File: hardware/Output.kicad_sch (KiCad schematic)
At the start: 26 parts, among them J11 Conn_Coaxial, J12 Conn_Coaxial, J13 Conn_Coaxial, J14 Conn_Coaxial, J15 Conn_Coaxial, J16 Conn_Coaxial, J17 Conn_Coaxial, J18 Conn_Coaxial, U31 74LVCH2T45DC, U32 74LVCH2T45DC

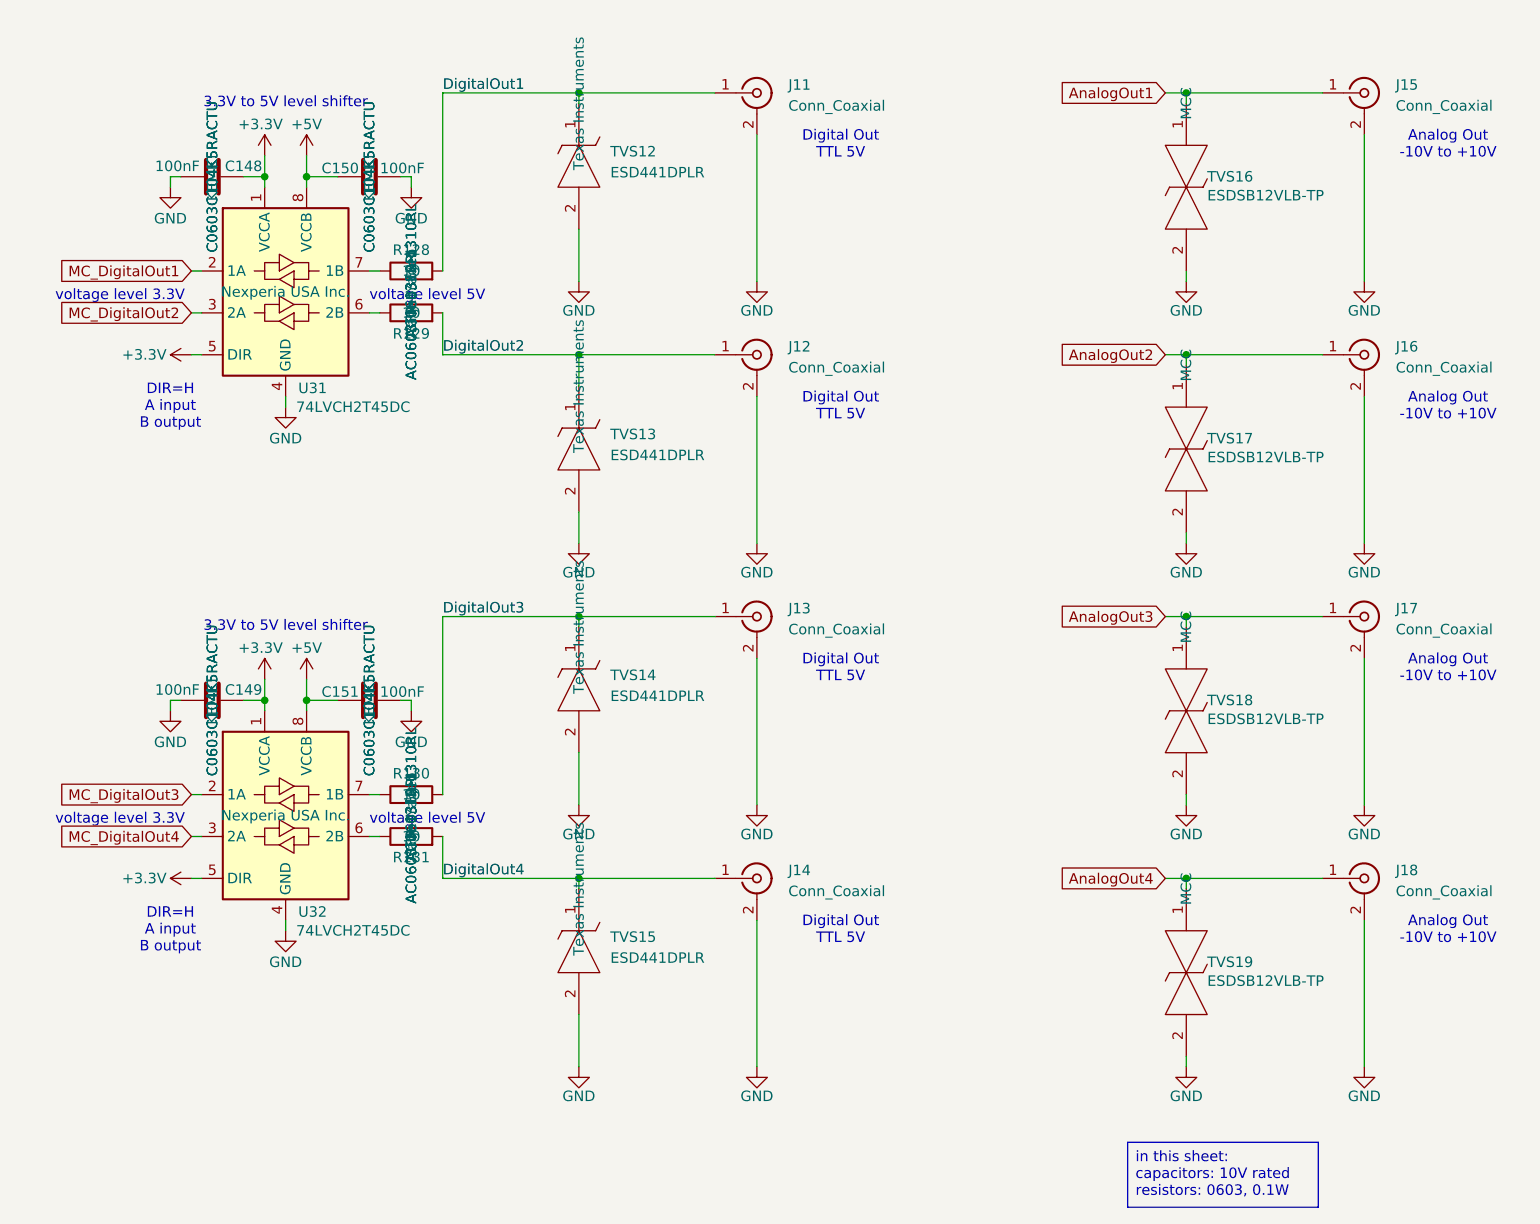
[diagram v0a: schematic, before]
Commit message: Not necessary text is hidden + BOM on schematic
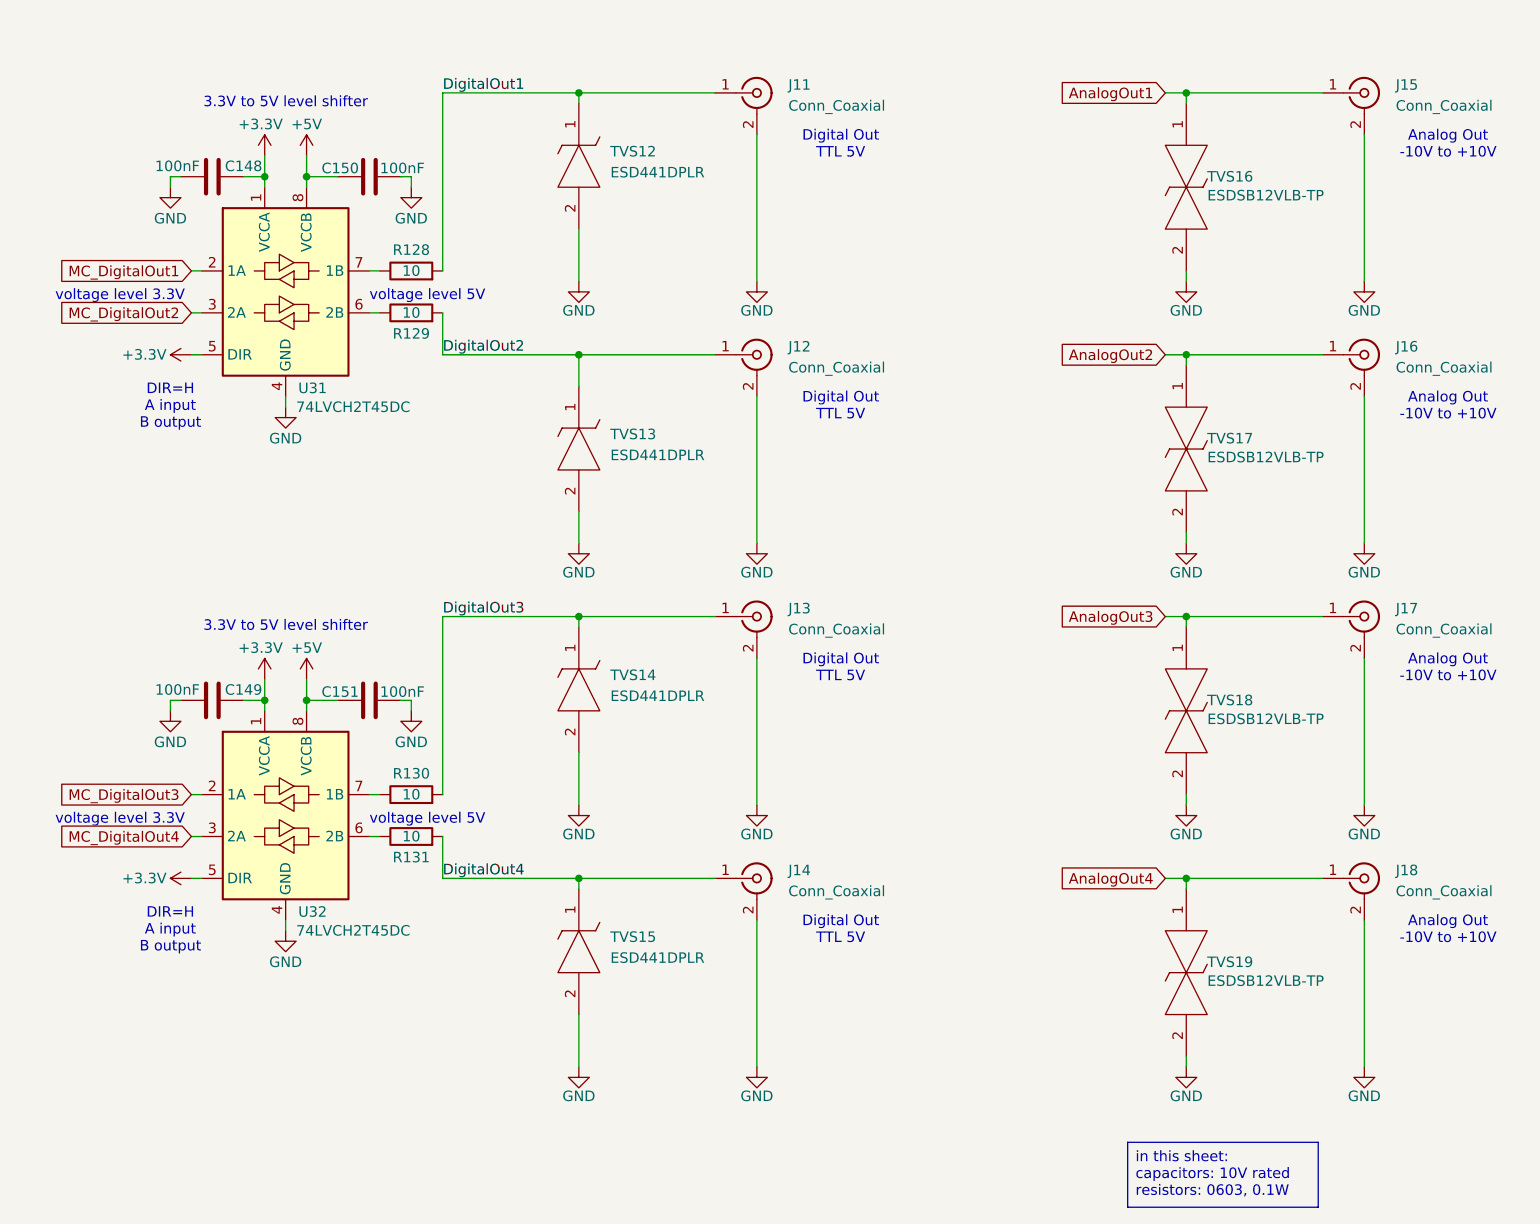
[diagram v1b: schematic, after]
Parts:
- C148, C149, C150, C151: Temperature Coefficient X7R -> (none)
- TVS12, TVS13, TVS14, TVS15: MPN (none) -> ESD441DPLR
- TVS16, TVS17, TVS18, TVS19: MPN (none) -> ESDSB12VLB-TP
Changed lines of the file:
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@@
 					(size 1.27 1.27)
 				)
+				(hide yes)
 			)
 		)
@@
 					(size 1.27 1.27)
 				)
+				(hide yes)
 			)
 		)
@@
 					(size 1.27 1.27)
 				)
+				(hide yes)
 			)
 		)
@@
 					(size 1.27 1.27)
 				)
+				(hide yes)
+			)
+		)
+		(property "MPN" "ESD441DPLR"
+			(at 110.49 95.25 0)
+			(effects
+				(font
+					(size 1.27 1.27)
+				)
+				(hide yes)
 			)
 		)
@@
 					(size 1.27 1.27)
 				)
+				(hide yes)
+			)
+		)
+		(property "MPN" "ESD441DPLR"
+			(at 110.49 31.75 0)
+			(effects
+				(font
+					(size 1.27 1.27)
+				)
+				(hide yes)
 			)
 		)
@@
 			)
 		)
-		(property "Temperature Coefficient" "X7R"
+		(property "Temperature Coefficient" ""
 			(at 85.09 40.64 0)
 			(effects
@@
 					(size 1.27 1.27)
 				)
+				(hide yes)
 			)
 		)
@@
 					(size 1.27 1.27)
 				)
+				(hide yes)
 			)
 		)
@@
 					(size 1.27 1.27)
 				)
+				(hide yes)
 			)
 		)
@@
 					(size 1.27 1.27)
 				)
+				(hide yes)
 			)
 		)
@@
 			)
 		)
-		(property "Temperature Coefficient" "X7R"
+		(property "Temperature Coefficient" ""
 			(at 66.04 40.64 0)
 			(effects
@@
 					(size 1.27 1.27)
 				)
+				(hide yes)
 			)
 		)
@@
 					(size 1.27 1.27)
 				)
+				(hide yes)
 			)
 		)
@@
 					(size 1.27 1.27)
 				)
+				(hide yes)
 			)
 		)
@@
 					(size 1.27 1.27)
 				)
+				(hide yes)
 			)
 		)
@@
 					(size 1.27 1.27)
 				)
+				(hide yes)
+			)
+		)
+		(property "MPN" "ESD441DPLR"
+			(at 110.49 127 0)
+			(effects
+				(font
+					(size 1.27 1.27)
+				)
+				(hide yes)
 			)
 		)
@@
 					(size 1.27 1.27)
 				)
+				(hide yes)
+			)
+		)
+		(property "MPN" "ESDSB12VLB-TP"
+			(at 184.15 95.25 0)
+			(effects
+				(font
+					(size 1.27 1.27)
+				)
+				(hide yes)
 			)
 		)
@@
 					(size 1.27 1.27)
 				)
+				(hide yes)
 			)
 		)
@@
 					(size 1.27 1.27)
 				)
+				(hide yes)
 			)
 		)
@@
 					(size 1.27 1.27)
 				)
+				(hide yes)
 			)
 		)
@@
 					(size 1.27 1.27)
 				)
+				(hide yes)
+			)
+		)
+		(property "MPN" "ESDSB12VLB-TP"
+			(at 184.15 31.75 0)
+			(effects
+				(font
+					(size 1.27 1.27)
+				)
+				(hide yes)
 			)
 		)
@@
 			)
 		)
-		(property "Temperature Coefficient" "X7R"
+		(property "Temperature Coefficient" ""
 			(at 66.04 104.14 0)
 			(effects
@@
 					(size 1.27 1.27)
 				)
+				(hide yes)
 			)
 		)
@@
 					(size 1.27 1.27)
 				)
+				(hide yes)
 			)
 		)
@@
 					(size 1.27 1.27)
 				)
+				(hide yes)
 			)
 		)
@@
 					(size 1.27 1.27)
 				)
+				(hide yes)
 			)
 		)
@@
 					(size 1.27 1.27)
 				)
+				(hide yes)
 			)
 		)
@@
 					(size 1.27 1.27)
 				)
+				(hide yes)
 			)
 		)
@@
 					(size 1.27 1.27)
 				)
+				(hide yes)
+			)
+		)
+		(property "MPN" "ESDSB12VLB-TP"
+			(at 184.15 127 0)
+			(effects
+				(font
+					(size 1.27 1.27)
+				)
+				(hide yes)
 			)
 		)
@@
 			)
 		)
-		(property "Temperature Coefficient" "X7R"
+		(property "Temperature Coefficient" ""
 			(at 85.09 104.14 0)
 			(effects
@@
 					(size 1.27 1.27)
 				)
+				(hide yes)
 			)
 		)
@@
 					(size 1.27 1.27)
 				)
+				(hide yes)
 			)
 		)
@@
 					(size 1.27 1.27)
 				)
+				(hide yes)
 			)
 		)
@@
 					(size 1.27 1.27)
 				)
+				(hide yes)
+			)
+		)
+		(property "MPN" "ESDSB12VLB-TP"
+			(at 184.15 63.5 0)
+			(effects
+				(font
+					(size 1.27 1.27)
+				)
+				(hide yes)
 			)
 		)
@@
 					(size 1.27 1.27)
 				)
+				(hide yes)
 			)
 		)
@@
 					(size 1.27 1.27)
 				)
+				(hide yes)
 			)
 		)
@@
 					(size 1.27 1.27)
 				)
+				(hide yes)
 			)
 		)
@@
 					(size 1.27 1.27)
 				)
+				(hide yes)
+			)
+		)
+		(property "MPN" "ESD441DPLR"
+			(at 110.49 66.04 0)
+			(effects
+				(font
+					(size 1.27 1.27)
+				)
+				(hide yes)
 			)
 		)

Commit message: BOM cont.
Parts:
- J11, J12, J13, J14, J15, J16, J17, J18: MPN (none) -> CONSMA002-SMD-G-T; Manufacturer TE Connectivity Linx -> TE Connectivity Linx; Manufacturer_Name (none) -> TE Connectivity Linx; Manufacturer_Part_Number (none) -> CONSMA002-SMD-G-T
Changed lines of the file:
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@@
 			)
 		)
-		(property "Manufacturer" " TE Connectivity Linx"
+		(property "Manufacturer" "TE Connectivity Linx"
 			(at 132.08 125.73 0)
 			(effects
@@
 		)
 		(property "Manufacturer Number" "CONSMA002-SMD-G-T"
+			(at 132.08 125.73 0)
+			(effects
+				(font
+					(size 1.27 1.27)
+				)
+				(hide yes)
+			)
+		)
+		(property "MPN" "CONSMA002-SMD-G-T"
+			(at 132.08 125.73 0)
+			(effects
+				(font
+					(size 1.27 1.27)
+				)
+				(hide yes)
+			)
+		)
+		(property "Manufacturer_Name" "TE Connectivity Linx"
+			(at 132.08 125.73 0)
+			(effects
+				(font
+					(size 1.27 1.27)
+				)
+				(hide yes)
+			)
+		)
+		(property "Manufacturer_Part_Number" "CONSMA002-SMD-G-T"
 			(at 132.08 125.73 0)
 			(effects
@@
 			)
 		)
-		(property "Manufacturer" " TE Connectivity Linx"
+		(property "Manufacturer" "TE Connectivity Linx"
 			(at 205.74 62.23 0)
 			(effects
@@
 		)
 		(property "Manufacturer Number" "CONSMA002-SMD-G-T"
+			(at 205.74 62.23 0)
+			(effects
+				(font
+					(size 1.27 1.27)
+				)
+				(hide yes)
+			)
+		)
+		(property "MPN" "CONSMA002-SMD-G-T"
+			(at 205.74 62.23 0)
+			(effects
+				(font
+					(size 1.27 1.27)
+				)
+				(hide yes)
+			)
+		)
+		(property "Manufacturer_Name" "TE Connectivity Linx"
+			(at 205.74 62.23 0)
+			(effects
+				(font
+					(size 1.27 1.27)
+				)
+				(hide yes)
+			)
+		)
+		(property "Manufacturer_Part_Number" "CONSMA002-SMD-G-T"
 			(at 205.74 62.23 0)
 			(effects
@@
 			)
 		)
-		(property "Manufacturer" " TE Connectivity Linx"
+		(property "Manufacturer" "TE Connectivity Linx"
 			(at 205.74 125.73 0)
 			(effects
@@
 		)
 		(property "Manufacturer Number" "CONSMA002-SMD-G-T"
+			(at 205.74 125.73 0)
+			(effects
+				(font
+					(size 1.27 1.27)
+				)
+				(hide yes)
+			)
+		)
+		(property "MPN" "CONSMA002-SMD-G-T"
+			(at 205.74 125.73 0)
+			(effects
+				(font
+					(size 1.27 1.27)
+				)
+				(hide yes)
+			)
+		)
+		(property "Manufacturer_Name" "TE Connectivity Linx"
+			(at 205.74 125.73 0)
+			(effects
+				(font
+					(size 1.27 1.27)
+				)
+				(hide yes)
+			)
+		)
+		(property "Manufacturer_Part_Number" "CONSMA002-SMD-G-T"
 			(at 205.74 125.73 0)
 			(effects
@@
 			)
 		)
-		(property "Manufacturer" " TE Connectivity Linx"
+		(property "Manufacturer" "TE Connectivity Linx"
 			(at 132.08 62.23 0)
 			(effects
@@
 		)
 		(property "Manufacturer Number" "CONSMA002-SMD-G-T"
+			(at 132.08 62.23 0)
+			(effects
+				(font
+					(size 1.27 1.27)
+				)
+				(hide yes)
+			)
+		)
+		(property "MPN" "CONSMA002-SMD-G-T"
+			(at 132.08 62.23 0)
+			(effects
+				(font
+					(size 1.27 1.27)
+				)
+				(hide yes)
+			)
+		)
+		(property "Manufacturer_Name" "TE Connectivity Linx"
+			(at 132.08 62.23 0)
+			(effects
+				(font
+					(size 1.27 1.27)
+				)
+				(hide yes)
+			)
+		)
+		(property "Manufacturer_Part_Number" "CONSMA002-SMD-G-T"
 			(at 132.08 62.23 0)
 			(effects
@@
 			)
 		)
-		(property "Manufacturer" " TE Connectivity Linx"
+		(property "Manufacturer" "TE Connectivity Linx"
 			(at 132.08 93.98 0)
 			(effects
@@
 		)
 		(property "Manufacturer Number" "CONSMA002-SMD-G-T"
+			(at 132.08 93.98 0)
+			(effects
+				(font
+					(size 1.27 1.27)
+				)
+				(hide yes)
+			)
+		)
+		(property "MPN" "CONSMA002-SMD-G-T"
+			(at 132.08 93.98 0)
+			(effects
+				(font
+					(size 1.27 1.27)
+				)
+				(hide yes)
+			)
+		)
+		(property "Manufacturer_Name" "TE Connectivity Linx"
+			(at 132.08 93.98 0)
+			(effects
+				(font
+					(size 1.27 1.27)
+				)
+				(hide yes)
+			)
+		)
+		(property "Manufacturer_Part_Number" "CONSMA002-SMD-G-T"
 			(at 132.08 93.98 0)
 			(effects
@@
 			)
 		)
-		(property "Manufacturer" " TE Connectivity Linx"
+		(property "Manufacturer" "TE Connectivity Linx"
 			(at 205.74 93.98 0)
 			(effects
@@
 		)
 		(property "Manufacturer Number" "CONSMA002-SMD-G-T"
+			(at 205.74 93.98 0)
+			(effects
+				(font
+					(size 1.27 1.27)
+				)
+				(hide yes)
+			)
+		)
+		(property "MPN" "CONSMA002-SMD-G-T"
+			(at 205.74 93.98 0)
+			(effects
+				(font
+					(size 1.27 1.27)
+				)
+				(hide yes)
+			)
+		)
+		(property "Manufacturer_Name" "TE Connectivity Linx"
+			(at 205.74 93.98 0)
+			(effects
+				(font
+					(size 1.27 1.27)
+				)
+				(hide yes)
+			)
+		)
+		(property "Manufacturer_Part_Number" "CONSMA002-SMD-G-T"
 			(at 205.74 93.98 0)
 			(effects
@@
 			)
 		)
-		(property "Manufacturer" " TE Connectivity Linx"
+		(property "Manufacturer" "TE Connectivity Linx"
 			(at 132.08 30.48 0)
 			(effects
@@
 		)
 		(property "Manufacturer Number" "CONSMA002-SMD-G-T"
+			(at 132.08 30.48 0)
+			(effects
+				(font
+					(size 1.27 1.27)
+				)
+				(hide yes)
+			)
+		)
+		(property "MPN" "CONSMA002-SMD-G-T"
+			(at 132.08 30.48 0)
+			(effects
+				(font
+					(size 1.27 1.27)
+				)
+				(hide yes)
+			)
+		)
+		(property "Manufacturer_Name" "TE Connectivity Linx"
+			(at 132.08 30.48 0)
+			(effects
+				(font
+					(size 1.27 1.27)
+				)
+				(hide yes)
+			)
+		)
+		(property "Manufacturer_Part_Number" "CONSMA002-SMD-G-T"
 			(at 132.08 30.48 0)
 			(effects
@@
 			)
 		)
-		(property "Manufacturer" " TE Connectivity Linx"
+		(property "Manufacturer" "TE Connectivity Linx"
 			(at 205.74 30.48 0)
 			(effects
@@
 			(at 205.74 30.48 0)
 			(effects
+				(font
+					(size 1.27 1.27)
+				)
+				(hide yes)
+			)
+		)
+		(property "MPN" "CONSMA002-SMD-G-T"
+			(at 205.74 30.48 0)
+			(effects
+				(font
+					(size 1.27 1.27)
+				)
+				(hide yes)
+			)
+		)
+		(property "Manufacturer_Name" "TE Connectivity Linx"
+			(at 205.74 30.48 0)
+			(effects
+				(font
+					(size 1.27 1.27)
+				)
+				(hide yes)
+			)
+		)
+		(property "Manufacturer_Part_Number" "CONSMA002-SMD-G-T"
+			(at 205.74 30.48 0)
+			(effects

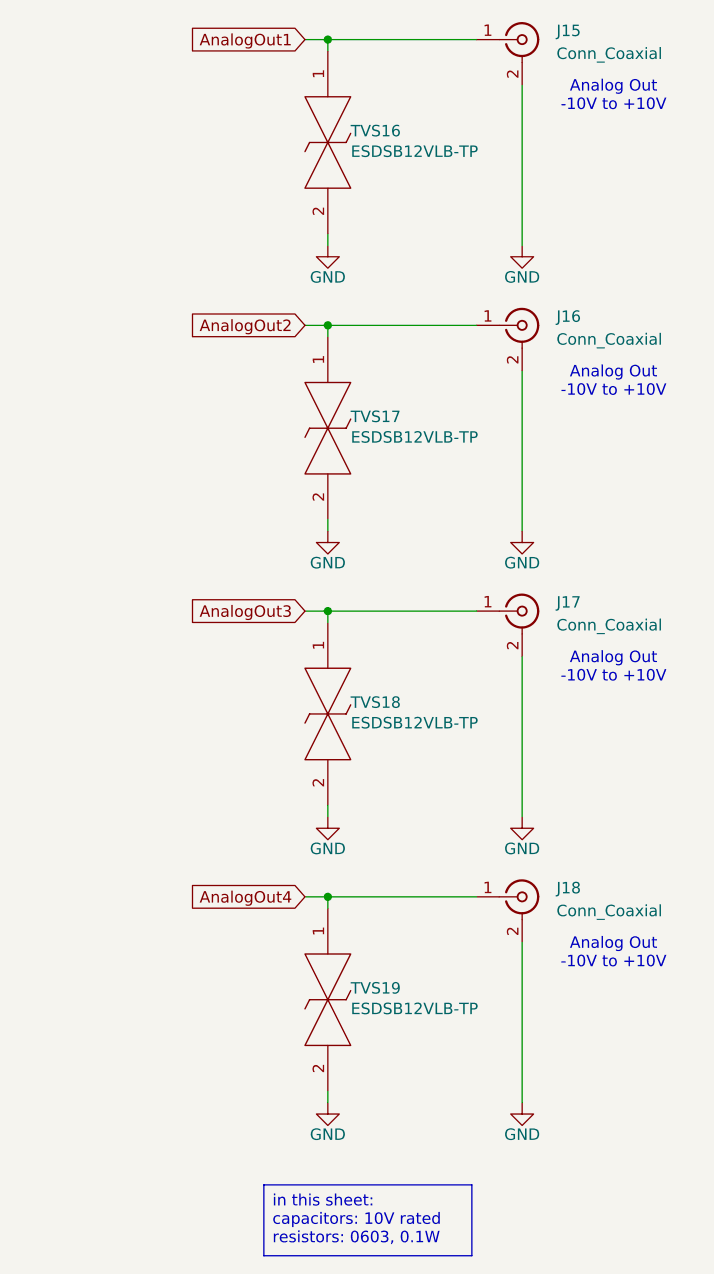
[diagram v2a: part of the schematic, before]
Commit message: TVS16,TVS17,TVS18,TVS19 parts have been changed from ESDSB12VLB-TP to PESD12VL1BSLAZ
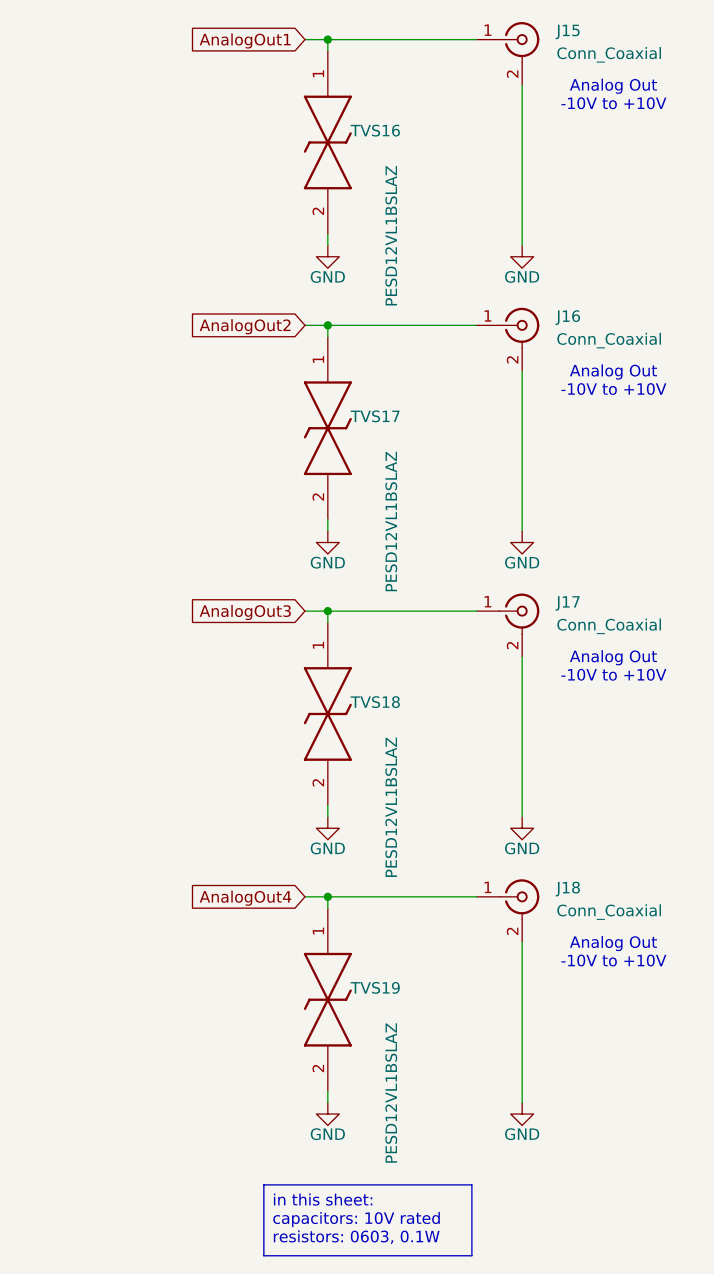
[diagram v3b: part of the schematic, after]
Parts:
- TVS16, TVS17, TVS18, TVS19: value ESDSB12VLB-TP -> PESD12VL1BSLAZ; footprint harp.device.quad.dac.kicad:ESDSB12VLBTP -> harp.device.quad.dac.kicad:PESD12VL1BSLAZ; symbol harp.device.quad.dac:ESDSB12VLB-TP -> harp.device.quad.dac:PESD12VL1BSLAZ; Arrow Part Number (none) -> PESD12VL1BSLAZ; Arrow Price/Stock (none) -> https://www.arrow.com/en/products/pesd12vl1bslaz/nexperia?r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; Height 0.55 -> 0.45; Manufacturer_Name MCC -> Nexperia; Manufacturer_Part_Number ESDSB12VLB-TP -> PESD12VL1BSLAZ; Mouser Part Number (none) -> 771-PESD12VL1BSLAZ; Mouser Price/Stock (none) -> https://www.mouser.co.uk/ProductDetail/Nexperia/PESD12VL1BS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
